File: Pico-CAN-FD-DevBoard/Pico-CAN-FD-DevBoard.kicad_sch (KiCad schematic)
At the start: 53 parts, among them CN1 SM04B-SRSS-TB (LF)(SN), CN2 2601-1102, CN3 2601-1102, J1 Conn_01x03, J2 Conn_01x08, J3 USB_C_Receptacle_USB2.0_14P, SW1 SW_Push, SW2 SW_Push, U1 RP2350B, U2 MCP251863T-H-SS, U3 W25Q128JVS, U4 W25Q128JVS, U5 ESD2CAN24DBZRQ1, U6 TPS51386RJNR, Y1 ABM8-272-T3, Y2 Crystal 40MHz

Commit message: changed stuff
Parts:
- added CN4: 2604-1102, easyeda2kicad:CONN-TH_2604-1102, symbol easyeda2kicad:2604-1102
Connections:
- net CAN_H: now also CN2.1, CN3.1
- net CAN_L: now also CN2.2, CN3.2
- net GND: now also CN4.1
- new net +12V: CN4.2
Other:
- moved on the sheet: CN1, CN2, CN3, R12, R13

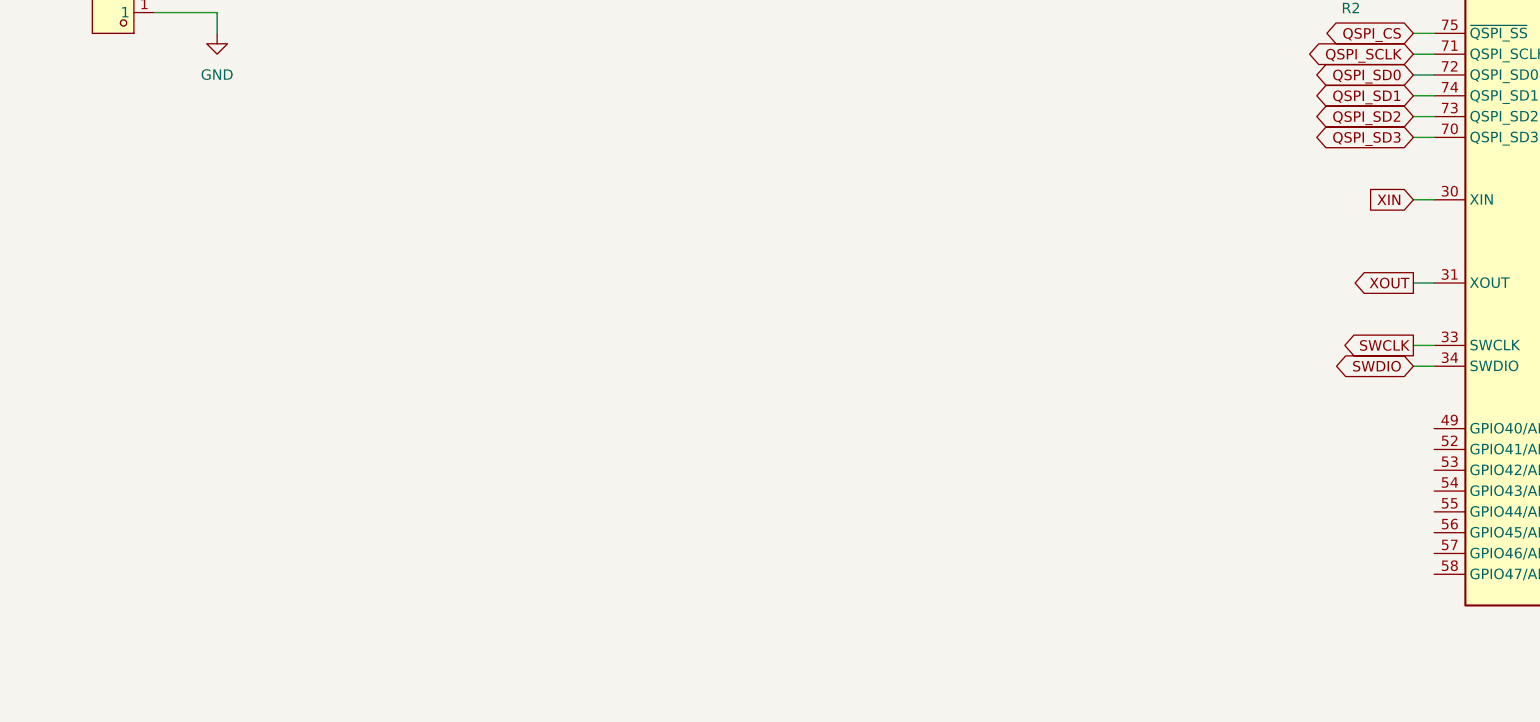
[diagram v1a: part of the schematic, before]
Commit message: added adc pins
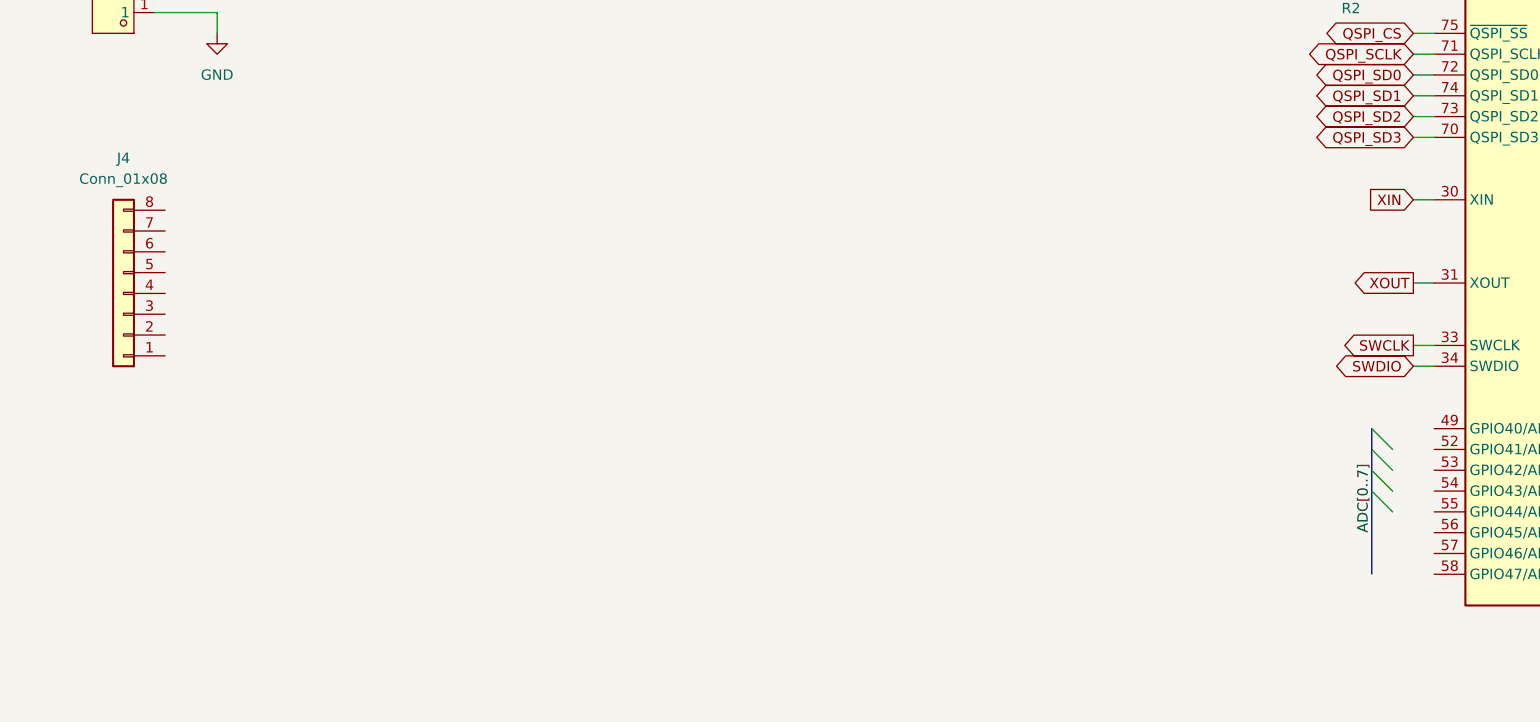
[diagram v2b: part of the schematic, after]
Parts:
- added J4: Conn_01x08, symbol Connector_Generic:Conn_01x08
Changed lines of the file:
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@@
 	)
 	(bus_entry
+		(at 177.8 185.42)
+		(size 2.54 2.54)
+		(stroke
+			(width 0)
+			(type default)
+		)
+	)
+	(bus_entry
 		(at 264.16 116.84)
 		(size 2.54 2.54)
@@
 	)
 	(bus_entry
+		(at 177.8 193.04)
+		(size 2.54 2.54)
+		(stroke
+			(width 0)
+			(type default)
+		)
+	)
+	(bus_entry
 		(at 264.16 119.38)
 		(size 2.54 2.54)
@@
 	)
 	(bus_entry
+		(at 177.8 190.5)
+		(size 2.54 2.54)
+		(stroke
+			(width 0)
+			(type default)
+		)
+	)
+	(bus_entry
 		(at 264.16 114.3)
 		(size 2.54 2.54)
@@
 		)
 	)
+	(bus_entry
+		(at 177.8 187.96)
+		(size 2.54 2.54)
+		(stroke
+			(width 0)
+			(type default)
+		)
+	)
 	(wire
 		(pts
@@
 		)
 	)
+	(bus
+		(pts
+			(xy 177.8 187.96) (xy 177.8 190.5)
+		)
+		(stroke
+			(width 0)
+			(type default)
+		)
+	)
 	(wire
 		(pts
@@
 		)
 	)
+	(bus
+		(pts
+			(xy 177.8 185.42) (xy 177.8 187.96)
+		)
+		(stroke
+			(width 0)
+			(type default)
+		)
+	)
 	(wire
 		(pts
@@
 	(bus
 		(pts
+			(xy 177.8 193.04) (xy 177.8 203.2)
+		)
+		(stroke
+			(width 0)
+			(type default)
+		)
+	)
+	(bus
+		(pts
 			(xy 266.7 116.84) (xy 266.7 119.38)
 		)
@@
 		)
 	)
+	(bus
+		(pts
+			(xy 177.8 190.5) (xy 177.8 193.04)
+		)
+		(stroke
+			(width 0)
+			(type default)
+		)
+	)
 	(wire
 		(pts
@@
 		)
 	)
+	(label "ADC[0..7]"
+		(at 177.8 198.12 90)
+		(effects
+			(font
+				(size 1.27 1.27)
+			)
+			(justify left bottom)
+		)
+	)
 	(label "NPXL_3V3_4"
 		(at 252.73 124.46 0)
@@
 					(unit 1)
 				)
+			)
+		)
+	)
+	(symbol
+		(lib_id "Connector_Generic:Conn_01x08")
+		(at 25.4 168.91 180)
+		(unit 1)
+		(exclude_from_sim no)
+		(in_bom yes)
+		(on_board yes)
+		(dnp no)
+		(fields_autoplaced yes)
+		(property "Reference" "J4"
+			(at 25.4 152.4 0)
+			(effects
+				(font
+					(size 1.27 1.27)
+				)
+			)
+		)
+		(property "Value" "Conn_01x08"
+			(at 25.4 154.94 0)
+			(effects
+				(font
+					(size 1.27 1.27)
+				)
+			)
+		)
+		(property "Footprint" ""
+			(at 25.4 168.91 0)
+			(effects
+				(font
+					(size 1.27 1.27)
+				)
+				(hide yes)
+			)
+		)
+		(property "Datasheet" "~"
+			(at 25.4 168.91 0)
+			(effects
+				(font
+					(size 1.27 1.27)
+				)
+				(hide yes)
+			)
+		)
+		(property "Description" "Generic connector, single row, 01x08, script generated (kicad-library-utils/schlib/autogen/connector/)"
+			(at 25.4 168.91 0)
+			(effects
+				(font
+					(size 1.27 1.27)
+				)
+				(hide yes)
+			)
+		)
+		(pin "3"
+		)
+		(pin "8"
+		)
+		(pin "7"
+		)
+		(pin "6"
+		)
+		(pin "5"
+		)
+		(pin "2"
+		)
+		(pin "4"
+		)
+		(pin "1"
+		)
+		(instances
+			(project ""
+				(path "/a8df20cc-31fb-4360-ac7f-9e5ea21059e1"
+					(reference "J4")
+					(unit 1)
+				)
